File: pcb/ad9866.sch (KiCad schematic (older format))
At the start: 71 parts, among them CN1 MEC6-140_CONNECTOR_BEMICRO, CN2 PCIE, P1 CONN_4, P10 CONN_1, P13 CONN_1, P14 CONN_1, P15 Si510 73.728, P16 CONN_3X2, P17 CONN_4, P18 CONN_1, P19 CONN_1, P2 CONN_1, P20 CONN_1, P22 CONN_1, P23 CONN_5, P24 CONN_5, P25 CONN_5, P3 CONN_1, P4 CONN_1, P5 CONN_1, P6 CONN_1, P8 CONN_1, P9 CONN_1, T1 TRANSF_ADT8, T2 TRANSF_ADT2, T3 TRANSF_ADT2, U1 AD9866BCPZ, U2 NCP1117ST33T3G, U3 NCP1117ST33T3G

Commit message: Changed schematic and .cmp for issues 12 & 16-20
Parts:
- removed CN2: PCIE, symbol PCIE
- removed P1, P17: CONN_4, symbol CONN_4
- removed P16: CONN_3X2, symbol CONN_3X2
- removed P18, P2, P3, P4, P5: CONN_1, symbol CONN_1
- removed R3, R4, R5: 10K, symbol R
- added P1: CONN_2, symbol CONN_2
- C1, C10, C11, C12, C13, C14, C15, C16, C2, C21, C23, C24, C25, C26, C27, C28, C29, C3, C30, C4, C5, C6, C7, C8, C9: symbol CSMALL -> Csmall
- C17, C18, C19, C20, C22: symbol CPSMALL -> CPsmall
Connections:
- net labels added: CLKOUT1
- wire segments 332 -> 310
- no-connect marks 0 -> 30

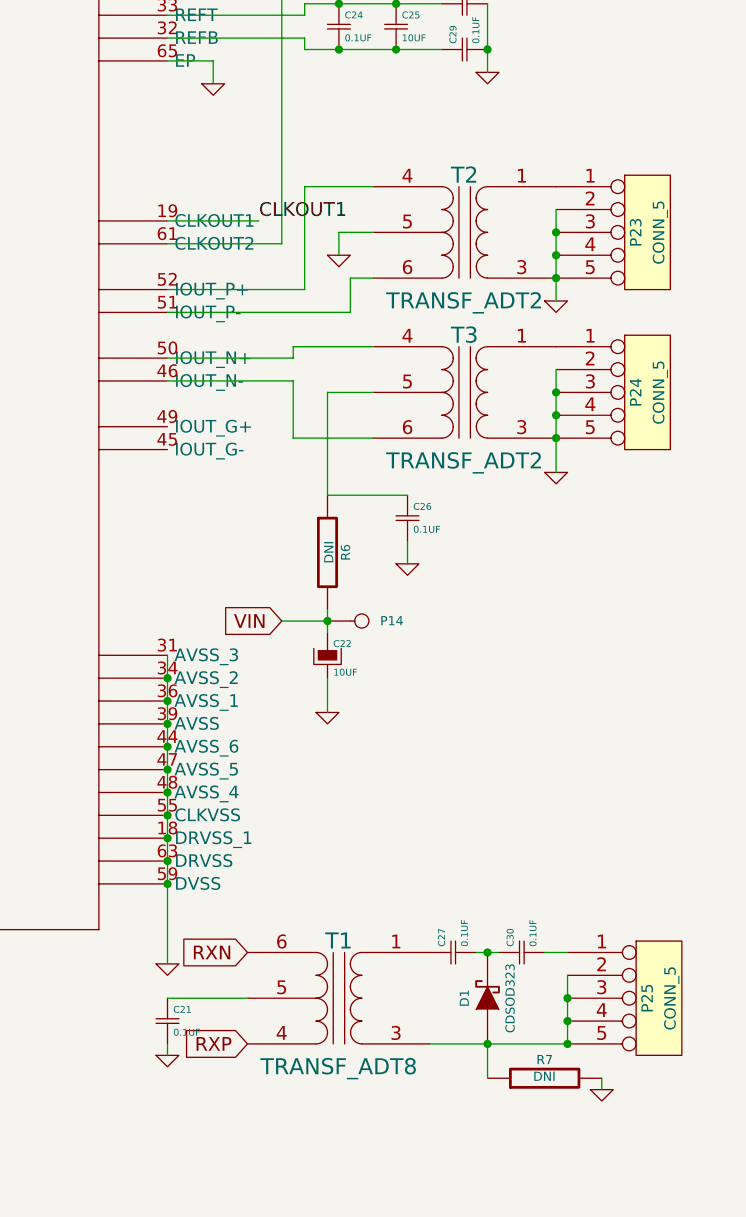
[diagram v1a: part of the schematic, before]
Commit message: Changed the SMA to SMA edge connectors, because then they are the same as the other board, and to get around the slight possibility the holes still are not right.
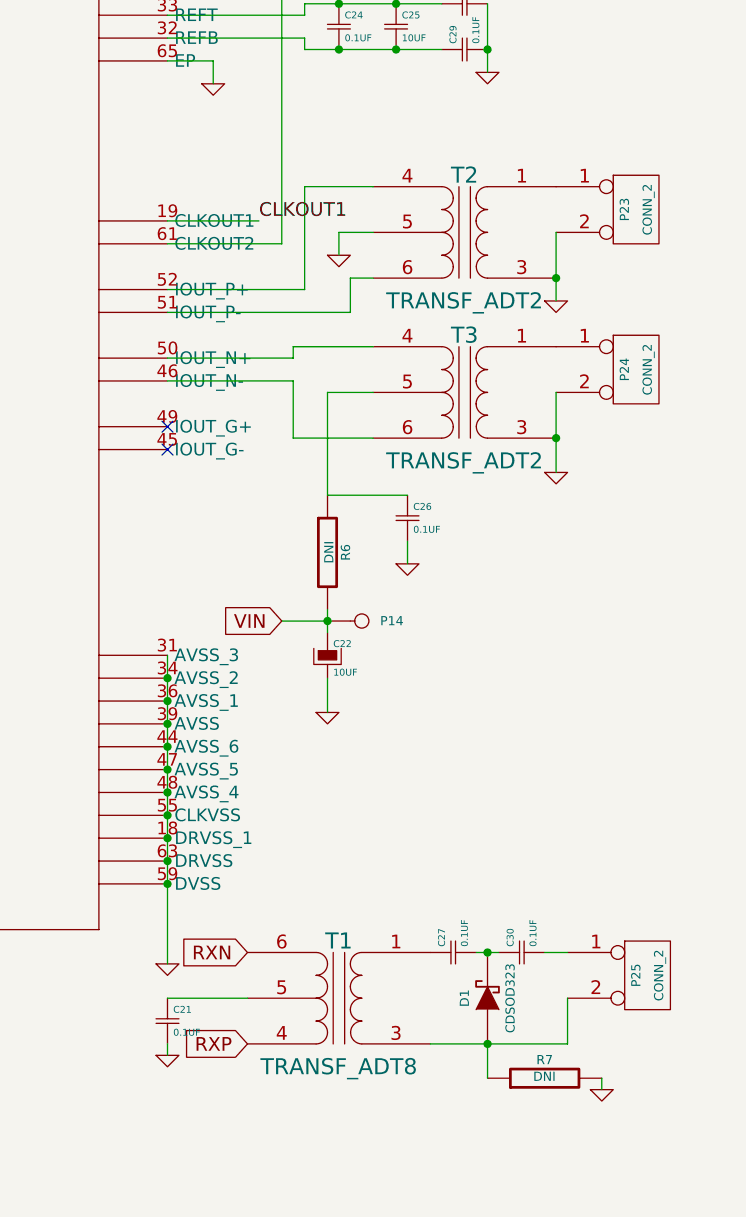
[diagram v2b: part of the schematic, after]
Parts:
- removed P23, P24, P25: CONN_5, symbol CONN_5
- added P23, P24, P25: CONN_2, symbol CONN_2
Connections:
- net GND: now also P23.2 (PM), P24.2 (PM)
- net at C30.2: now also P25.1 (P1)
- net at D1.1 (A), R7.1, T1.3 (S1): now also P25.2 (PM)
- net at T2.1 (S2): now also P23.1 (P1)
- net at T3.1 (S2): now also P24.1 (P1)
- no-connect marks 30 -> 32
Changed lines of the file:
@@
-$EndComp
-$Comp
-L CONN_5 P23
-U 1 1 52D6C777
-P 11000 2700
-F 0 "P23" V 10950 2700 50  0000 C CNN
-F 1 "CONN_5" V 11050 2700 50  0000 C CNN
-F 2 "" H 11000 2700 60  0000 C CNN
-F 3 "" H 11000 2700 60  0000 C CNN
-	1    11000 2700
-	1    0    0    -1
-$EndComp
-$Comp
-L CONN_5 P24
-U 1 1 52D6C8B5
-P 11000 3400
-F 0 "P24" V 10950 3400 50  0000 C CNN
-F 1 "CONN_5" V 11050 3400 50  0000 C CNN
-F 2 "" H 11000 3400 60  0000 C CNN
-F 3 "" H 11000 3400 60  0000 C CNN
-	1    11000 3400
-	1    0    0    -1
-$EndComp
-$Comp
-L CONN_5 P25
-U 1 1 52D6CA0C
-P 11050 6050
-F 0 "P25" V 11000 6050 50  0000 C CNN
-F 1 "CONN_5" V 11100 6050 50  0000 C CNN
-F 2 "" H 11050 6050 60  0000 C CNN
-F 3 "" H 11050 6050 60  0000 C CNN
-	1    11050 6050
-	1    0    0    -1
 $EndComp
 $Comp
@@
 Connection ~ 10600 2900
 Wire Wire Line
-	10600 2600 10600 3000
-Connection ~ 10600 2700
-Connection ~ 10600 2800
-Wire Wire Line
-	10600 3300 10600 3750
-Connection ~ 10600 3400
-Connection ~ 10600 3500
-Wire Wire Line
 	10650 6250 10050 6250
 Wire Wire Line
@@
 Wire Wire Line
 	10800 6400 10800 6450
-Wire Wire Line
-	10650 5950 10650 6250
-Connection ~ 10650 6050
-Connection ~ 10650 6150
-Connection ~ 10650 6250
 Wire Wire Line
 	4150 4600 4150 5600
@@
 NoConn ~ 1750 4700
 NoConn ~ 1750 4800
+NoConn ~ 8900 3550
+NoConn ~ 8900 3650
+$Comp
+L CONN_2 P24
+U 1 1 53AC66E8
+P 10950 3300
+F 0 "P24" V 10900 3300 40  0000 C CNN
+F 1 "CONN_2" V 11000 3300 40  0000 C CNN
+F 2 "" H 10950 3300 60  0000 C CNN
+F 3 "" H 10950 3300 60  0000 C CNN
+	1    10950 3300
+	1    0    0    -1
+$EndComp
+Wire Wire Line
+	10600 3750 10600 3400
+$Comp
+L CONN_2 P23
+U 1 1 53AC6A3D
+P 10950 2600
+F 0 "P23" V 10900 2600 40  0000 C CNN
+F 1 "CONN_2" V 11000 2600 40  0000 C CNN
+F 2 "" H 10950 2600 60  0000 C CNN
+F 3 "" H 10950 2600 60  0000 C CNN
+	1    10950 2600
+	1    0    0    -1
+$EndComp
+Wire Wire Line
+	10600 3000 10600 2700
+$Comp
+L CONN_2 P25
+U 1 1 53AC7360
+P 11000 5950
+F 0 "P25" V 10950 5950 40  0000 C CNN
+F 1 "CONN_2" V 11050 5950 40  0000 C CNN
+F 2 "" H 11000 5950 60  0000 C CNN
+F 3 "" H 11000 5950 60  0000 C CNN
+	1    11000 5950
+	1    0    0    -1
+$EndComp
+Wire Wire Line
+	10650 6250 10650 6050
 $EndSCHEMATC

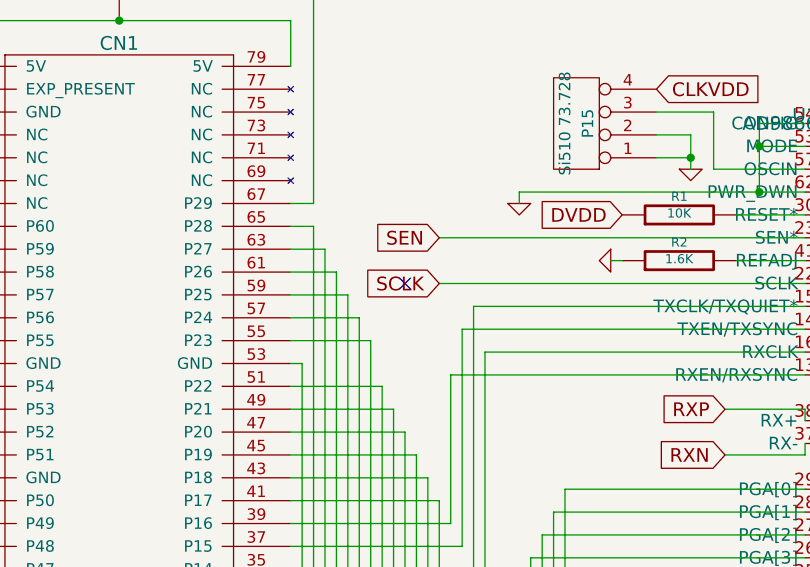
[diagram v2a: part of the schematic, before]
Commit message: Added the bottom ground plane in.
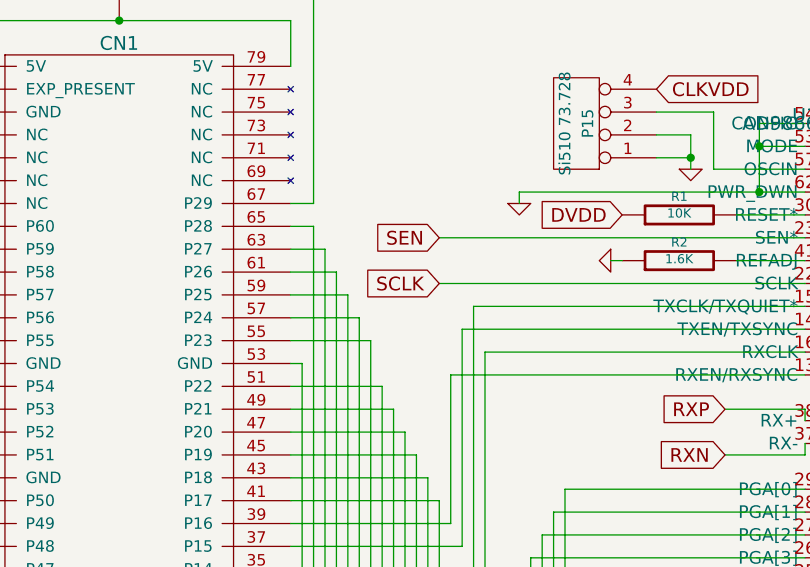
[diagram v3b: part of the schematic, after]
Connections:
- no-connect marks 32 -> 31
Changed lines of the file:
@@
 LIBS:ad9866c
 LIBS:ad9866
-LIBS:transf_minickts
-LIBS:con-pci_express(pci-e)
 LIBS:ad9866-cache
 EELAYER 24 0
@@
 $EndComp
 NoConn ~ 4150 3600
-NoConn ~ 3750 2050
 Text GLabel 1350 1600 0    60   Input ~ 0
 SEN
